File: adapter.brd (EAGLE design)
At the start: 47.9 x 48.2 mm, 28 parts, among them Q1 BS170, Q2 BS170, Q3 BS170, Q4 BS170, X2 KUSBVX

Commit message: letzte Anpassungen zum Ätzen
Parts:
- moved GPIO14 26.7 mm to (22.9, 43.2)
- moved GPIO15 26.7 mm to (25.4, 43.2)
- moved GPIO25 26.7 mm to (40.6, 43.2)
- moved GPIO4 26.7 mm to (22.9, 33.0)
- moved GPIO7 26.7 mm to (45.7, 43.2)
- moved GPIO9 26.7 mm to (40.6, 33.0)
- moved Q1 26.7 mm to (29.2, 25.4)
- moved Q2 26.7 mm to (29.2, 17.8)
- moved Q3 26.7 mm to (34.3, 25.4)
- moved Q4 26.7 mm to (34.3, 17.8)
- moved R1 26.7 mm to (25.4, 22.9)
- moved R2 26.7 mm to (25.4, 14.0)
- moved X2 26.7 mm to (50.8, 11.4)
- moved GPIO17 26.7 mm to (27.9, 33.0)
- moved GPIO18 26.7 mm to (27.9, 43.2)
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
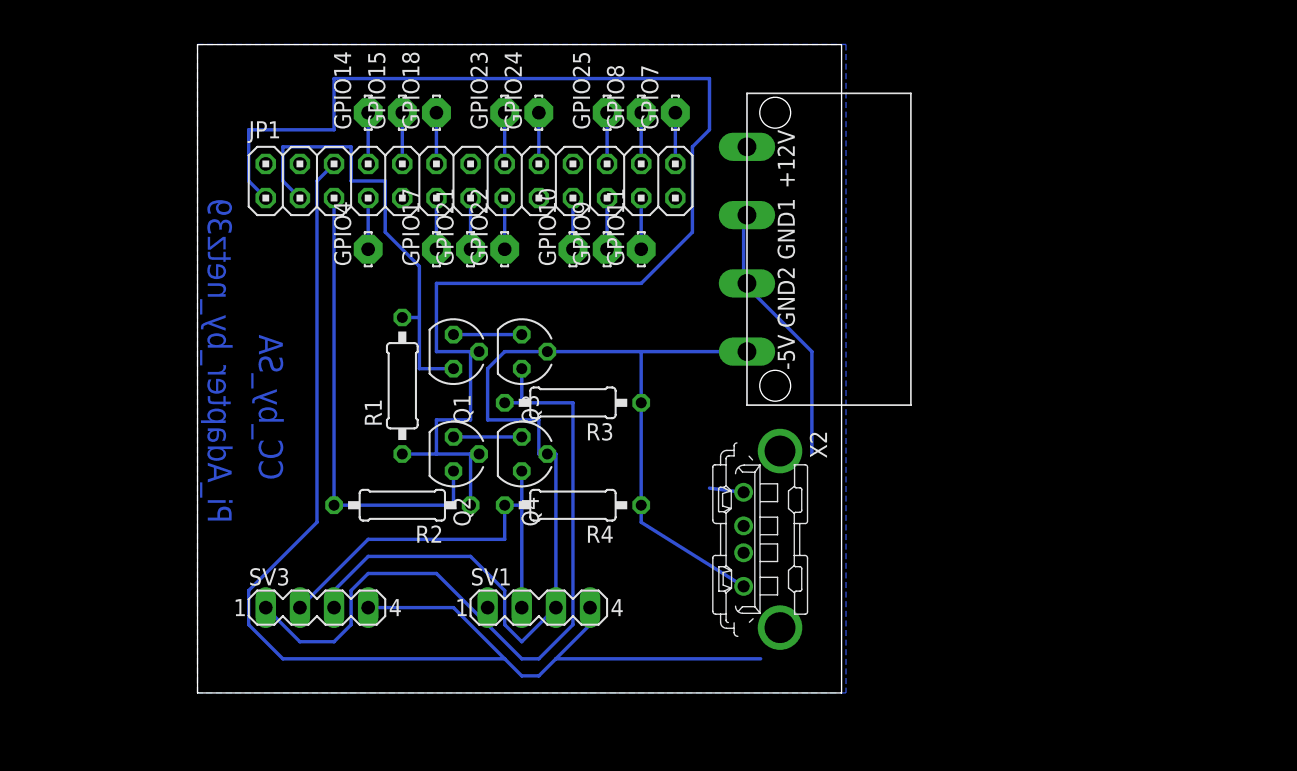
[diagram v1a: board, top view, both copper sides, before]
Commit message: Redesign (INT-Leitung und breitere Leitung für Spannungsversorgung)
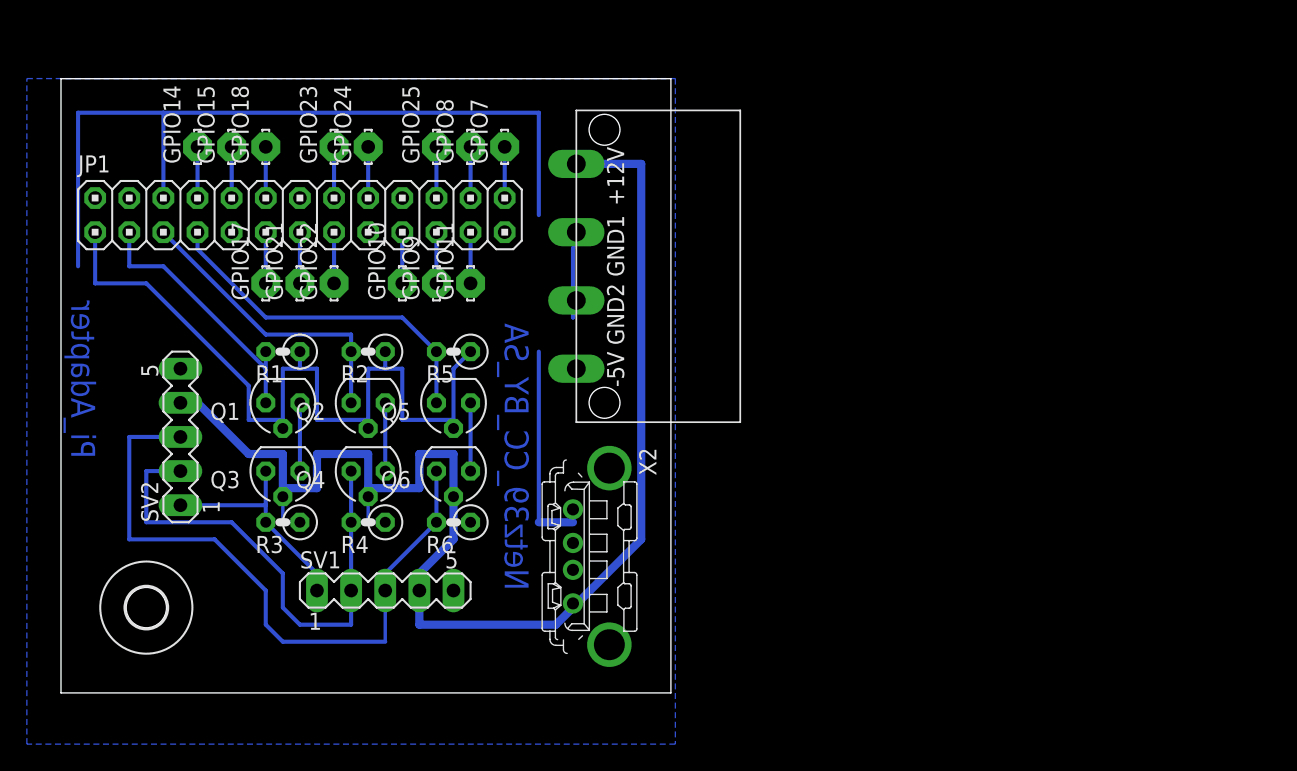
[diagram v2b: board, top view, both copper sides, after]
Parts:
- removed GPIO4: LSP10, solpad:LSP10
- removed SV3: (no value), con-lstb:MA04-1
- added Q5, Q6: BS170, transistor-small-signal:SOT54E
- added R5, R6: 10K, resistor:0207/2V
- added SV2: (no value), con-lstb:MA05-1
- added U$2: (no value), holes:3,0
- R1, R2, R3, R4: device resistor:0207/10 -> resistor:0207/2V
- SV1: device con-lstb:MA04-1 -> con-lstb:MA05-1
- moved R3 23.3 mm to (16.5, 12.7)
- moved Q3 19.9 mm to (16.5, 16.5), turned to 180 degrees
- moved R4 15.3 mm to (22.9, 12.7)
- moved Q1 13.3 mm to (16.5, 21.6), turned to 180 degrees
- moved GPIO10 13.0 mm to (25.4, 30.5)
- moved GPIO22 13.0 mm to (20.3, 30.5)
- moved GPIO23 13.0 mm to (20.3, 40.6)
- moved GPIO24 13.0 mm to (22.9, 40.6)
- moved GPIO17 13.0 mm to (15.2, 30.5)
- moved GPIO18 13.0 mm to (15.2, 40.6)
- moved GPIO11 13.0 mm to (30.5, 30.5)
- moved GPIO14 13.0 mm to (10.2, 40.6)
- moved GPIO15 13.0 mm to (12.7, 40.6)
- moved GPIO21 13.0 mm to (17.8, 30.5)
- moved GPIO25 13.0 mm to (27.9, 40.6)
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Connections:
- removed net GPIO4: GPIO4.MP, JP1.7
- new net INT3: JP1.7, Q5.S, R5.2
- new net INT5: Q6.S, R6.2, SV1.3, SV2.3
- new net N$17: Q5.D, Q6.D
- net GND: now also SV1.5, SV2.5; no longer SV1.4, SV3.4
- net SCL5: now also SV2.2; no longer SV3.2
- net SDA5: now also SV2.1; no longer SV3.1
- net VCC: now also Q6.G, R6.1, SV1.4, SV2.4, U$1.+12V; no longer SV1.3, SV3.3, U$1.-5V
- net VDD: now also Q5.G, R5.1
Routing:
- net INT5: track 0.00 -> 49.4 mm
- net VDD: track 104.2 -> 61.5 mm
- net SDA5: track 56.6 -> 16.8 mm
- net GND: track 116.7 -> 83.6 mm
- net INT3: track 0.00 -> 26.0 mm
- net VCC: track 88.4 -> 106.9 mm
- net SDA3: track 33.3 -> 19.7 mm
- net SCL3: track 34.3 -> 22.2 mm
- net SCL5: track 31.3 -> 37.7 mm
- net N$17: track 0.00 -> 5.08 mm
- net GPIO4: track 3.81 -> 0.00 mm
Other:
- board size 47.9 x 48.2 mm -> 45.4 x 45.7 mm
- board text added: "Netz39_CC_BY_SA"
- board text added: "Pi_Adapter"
- board text removed: "CC_by_SA"
- board text removed: "Pi_Adapter_by_netz39"

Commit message: Adapter: stecker angepasst Controller: board redesign
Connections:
- net VCC: now also U$1.-5V; no longer U$1.+12V
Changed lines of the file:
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@@
 <setting verticaltext="up"/>
 </settings>
-<grid distance="0.05" unitdist="inch" unit="inch" style="lines" multiple="1" display="no" altdistance="0.025" altunitdist="inch" altunit="inch"/>
+<grid distance="1.27" unitdist="mm" unit="mm" style="lines" multiple="1" display="no" altdistance="0.025" altunitdist="inch" altunit="inch"/>
 <layers>
 <layer number="1" name="Top" color="4" fill="1" visible="yes" active="yes"/>
@@
 <param name="mtCopper" value="0.035mm 0.035mm 0.035mm 0.035mm 0.035mm 0.035mm 0.035mm 0.035mm 0.035mm 0.035mm 0.035mm 0.035mm 0.035mm 0.035mm 0.035mm 0.035mm"/>
 <param name="mtIsolate" value="1.5mm 0.15mm 0.2mm 0.15mm 0.2mm 0.15mm 0.2mm 0.15mm 0.2mm 0.15mm 0.2mm 0.15mm 0.2mm 0.15mm 0.2mm"/>
-<param name="mdWireWire" value="10mil"/>
-<param name="mdWirePad" value="10mil"/>
-<param name="mdWireVia" value="10mil"/>
+<param name="mdWireWire" value="12mil"/>
+<param name="mdWirePad" value="12mil"/>
+<param name="mdWireVia" value="12mil"/>
 <param name="mdPadPad" value="10mil"/>
 <param name="mdPadVia" value="10mil"/>
@@
 <contactref element="R4" pad="1"/>
 <contactref element="Q6" pad="G"/>
-<contactref element="U$1" pad="+12V"/>
 <wire x1="22.86" y1="12.7" x2="22.86" y2="14.605" width="0.254" layer="16"/>
 <wire x1="24.13" y1="12.7" x2="22.86" y2="12.7" width="0.3048" layer="16"/>
@@
 <wire x1="26.67" y1="5.08" x2="36.83" y2="5.08" width="0.6096" layer="16"/>
 <wire x1="26.67" y1="7.62" x2="26.67" y2="5.08" width="0.6096" layer="16"/>
-<wire x1="43.18" y1="39.37" x2="38.35" y2="39.37" width="0.6096" layer="16"/>
 <wire x1="43.18" y1="11.43" x2="43.18" y2="39.37" width="0.6096" layer="16"/>
 <wire x1="38.1" y1="6.35" x2="43.18" y2="11.43" width="0.6096" layer="16"/>
@@
 <wire x1="29.21" y1="17.78" x2="26.67" y2="17.78" width="0.6096" layer="16"/>
 <wire x1="29.21" y1="14.605" x2="29.21" y2="17.78" width="0.6096" layer="16"/>
+<contactref element="U$1" pad="-5V"/>
+<wire x1="43.18" y1="39.37" x2="38.35" y2="39.37" width="0.6096" layer="16"/>
 </signal>
 <signal name="GND">
@@
 <wire x1="35.56" y1="35.56" x2="35.56" y2="43.18" width="0.3048" layer="16"/>
 <wire x1="38.1" y1="33.02" x2="38.35" y2="34.29" width="0.3048" layer="16"/>
-<polygon width="0.4064" layer="16">
+<polygon width="0.4064" layer="16" isolate="0.254">
 <vertex x="-2.54" y="45.72"/>
 <vertex x="45.72" y="45.72"/>
